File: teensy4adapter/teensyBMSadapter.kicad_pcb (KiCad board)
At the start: 2 copper layers, 23.2 x 37 mm, 11 parts, among them J1 Conn_01x14_Socket, J2 Conn_01x14_Pin, J3 Conn_01x14_Pin, J4 Conn_01x14_Socket

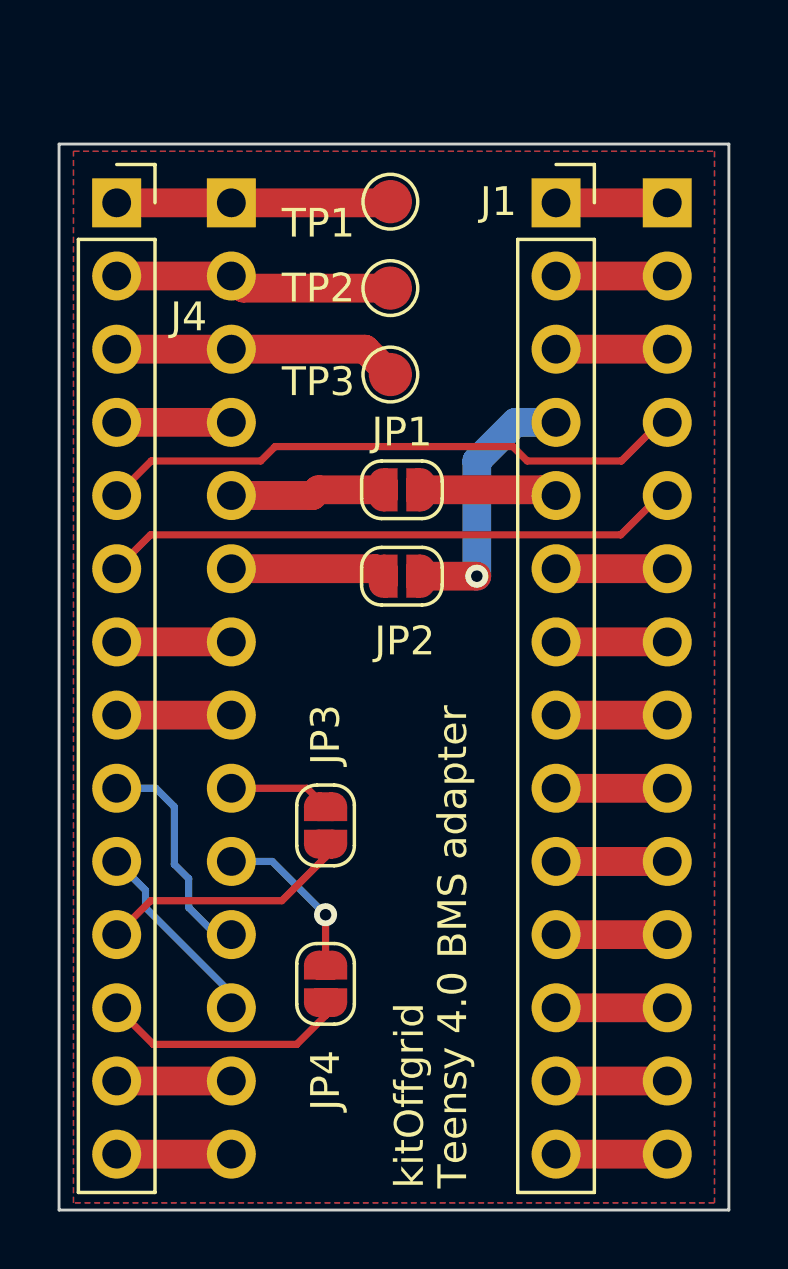
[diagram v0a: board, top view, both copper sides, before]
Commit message: kicad: connected UART3 because of the tesla module.
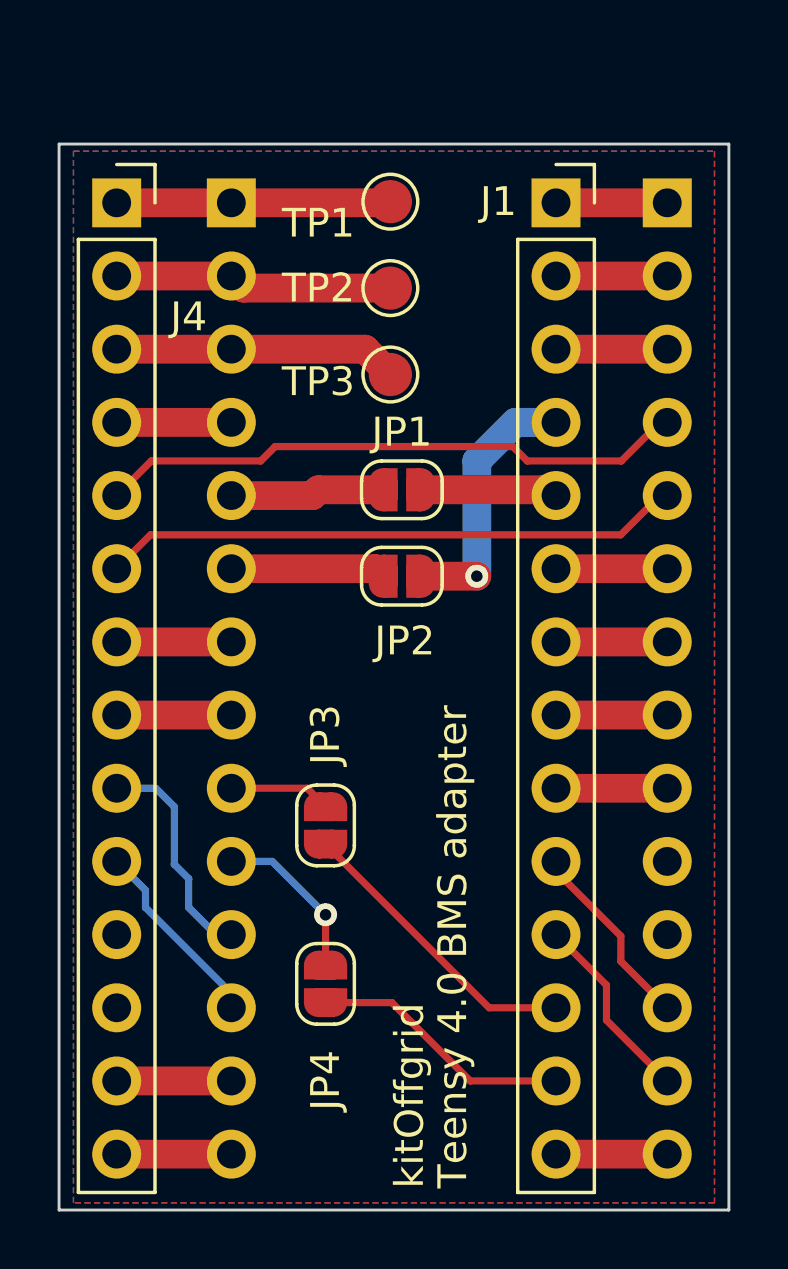
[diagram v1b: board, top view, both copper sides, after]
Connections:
- net Net-(J1-Pin_8) renamed /A5
- net Net-(J1-Pin_9) renamed /A4
- net Net-(J2-Pin_10) renamed /TX3
- net Net-(J2-Pin_9) renamed /RX3
- J1 pad 10: Net-(J1-Pin_10) -> /A3
- J1 pad 11: Net-(J1-Pin_11) -> /A2
- J1 pad 12: /A1 -> /RX3T4
- J1 pad 13: /A0 -> /TX3T4
- J3 pad 10: Net-(J1-Pin_10) -> /P17
- J3 pad 11: Net-(J1-Pin_11) -> /P18
- J3 pad 12: /A1 -> /A3
- J3 pad 13: /A0 -> /A2
- JP3 pad 1: /IO3 -> /RX3T4
- JP4 pad 1: /CS -> /TX3T4
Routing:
- net /RX3T4: track 0.00 -> 10.4 mm
- net /TX3T4: track 0.00 -> 9.13 mm
- net /IO3: track 8.81 -> 0.00 mm
- net /CS: track 8.64 -> 0.00 mm
- net /A3: track 0.00 -> 6.68 mm
- net /A2: track 0.00 -> 6.68 mm
- net Net-(J1-Pin_11): track 3.86 -> 0.00 mm
- net Net-(J1-Pin_10): track 3.86 -> 0.00 mm
- net /A1: track 3.86 -> 0.00 mm
- net /A0: track 3.86 -> 0.00 mm
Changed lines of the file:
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@@
   (net 6 "/A7")
   (net 7 "/A6")
-  (net 8 "Net-(J1-Pin_8)")
-  (net 9 "Net-(J1-Pin_9)")
-  (net 10 "Net-(J1-Pin_10)")
-  (net 11 "Net-(J1-Pin_11)")
-  (net 12 "/A1")
-  (net 13 "/A0")
+  (net 8 "/A5")
+  (net 9 "/A4")
+  (net 10 "/A3")
+  (net 11 "/A2")
+  (net 12 "/RX3T4")
+  (net 13 "/TX3T4")
   (net 14 "/LED{slash}SCK")
   (net 15 "/GND")
@@
   (net 29 "Net-(J2-Pin_5)")
   (net 30 "Net-(J2-Pin_6)")
-  (net 31 "Net-(J2-Pin_9)")
-  (net 32 "Net-(J2-Pin_10)")
+  (net 31 "/RX3")
+  (net 32 "/TX3")
+  (net 33 "/P17")
+  (net 34 "/P18")
   (footprint "Jumper:SolderJumper-2_P1.3mm_Open_RoundedPad1.0x1.5mm" (layer "F.Cu")
     (at 138.75 87.65 90)
@@
       (stroke (width 0.05) (type solid)) (layer "F.CrtYd"))
     (pad "1" smd custom (at -0.65 0 90) (size 1 0.5) (layers "F.Cu" "F.Mask")
-      (net 21 "/IO3") (pinfunction "A") (pintype "passive") (zone_connect 2) (thermal_bridge_angle 45)
+      (net 12 "/RX3T4") (pinfunction "A") (pintype "passive") (zone_connect 2) (thermal_bridge_angle 45)
       (options (clearance outline) (anchor rect))
       (primitives
@@
       ))
     (pad "2" smd custom (at 0.65 0 90) (size 1 0.5) (layers "F.Cu" "F.Mask")
-      (net 31 "Net-(J2-Pin_9)") (pinfunction "B") (pintype "passive") (zone_connect 2) (thermal_bridge_angle 45)
+      (net 31 "/RX3") (pinfunction "B") (pintype "passive") (zone_connect 2) (thermal_bridge_angle 45)
       (options (clearance outline) (anchor rect))
       (primitives
@@
       (stroke (width 0.05) (type solid)) (layer "F.CrtYd"))
     (pad "1" smd custom (at -0.65 0 90) (size 1 0.5) (layers "F.Cu" "F.Mask")
-      (net 22 "/CS") (pinfunction "A") (pintype "passive") (zone_connect 2) (thermal_bridge_angle 45)
+      (net 13 "/TX3T4") (pinfunction "A") (pintype "passive") (zone_connect 2) (thermal_bridge_angle 45)
       (options (clearance outline) (anchor rect))
       (primitives
@@
       ))
     (pad "2" smd custom (at 0.65 0 90) (size 1 0.5) (layers "F.Cu" "F.Mask")
-      (net 32 "Net-(J2-Pin_10)") (pinfunction "B") (pintype "passive") (zone_connect 2) (thermal_bridge_angle 45)
+      (net 32 "/TX3") (pinfunction "B") (pintype "passive") (zone_connect 2) (thermal_bridge_angle 45)
       (options (clearance outline) (anchor rect))
       (primitives
@@
       (net 7 "/A6") (pinfunction "Pin_7") (pintype "passive"))
     (pad "8" thru_hole oval (at 0 17.78) (size 1.7 1.7) (drill 1) (layers "*.Cu" "*.Mask")
-      (net 8 "Net-(J1-Pin_8)") (pinfunction "Pin_8") (pintype "passive"))
+      (net 8 "/A5") (pinfunction "Pin_8") (pintype "passive"))
     (pad "9" thru_hole oval (at 0 20.32) (size 1.7 1.7) (drill 1) (layers "*.Cu" "*.Mask")
-      (net 9 "Net-(J1-Pin_9)") (pinfunction "Pin_9") (pintype "passive"))
+      (net 9 "/A4") (pinfunction "Pin_9") (pintype "passive"))
     (pad "10" thru_hole oval (at 0 22.86) (size 1.7 1.7) (drill 1) (layers "*.Cu" "*.Mask")
-      (net 10 "Net-(J1-Pin_10)") (pinfunction "Pin_10") (pintype "passive"))
+      (net 10 "/A3") (pinfunction "Pin_10") (pintype "passive"))
     (pad "11" thru_hole oval (at 0 25.4) (size 1.7 1.7) (drill 1) (layers "*.Cu" "*.Mask")
-      (net 11 "Net-(J1-Pin_11)") (pinfunction "Pin_11") (pintype "passive"))
+      (net 11 "/A2") (pinfunction "Pin_11") (pintype "passive"))
     (pad "12" thru_hole oval (at 0 27.94) (size 1.7 1.7) (drill 1) (layers "*.Cu" "*.Mask")
-      (net 12 "/A1") (pinfunction "Pin_12") (pintype "passive"))
+      (net 12 "/RX3T4") (pinfunction "Pin_12") (pintype "passive"))
     (pad "13" thru_hole oval (at 0 30.48) (size 1.7 1.7) (drill 1) (layers "*.Cu" "*.Mask")
-      (net 13 "/A0") (pinfunction "Pin_13") (pintype "passive"))
+      (net 13 "/TX3T4") (pinfunction "Pin_13") (pintype "passive"))
     (pad "14" thru_hole oval (at 0 33.02) (size 1.7 1.7) (drill 1) (layers "*.Cu" "*.Mask")
       (net 14 "/LED{slash}SCK") (pinfunction "Pin_14") (pintype "passive"))
@@
       (net 20 "Net-(J2-Pin_8)") (pinfunction "Pin_8") (pintype "passive"))
     (pad "9" thru_hole oval (at 0 -20.32 180) (size 1.7 1.7) (drill 1) (layers "*.Cu" "*.Mask")
-      (net 31 "Net-(J2-Pin_9)") (pinfunction "Pin_9") (pintype "passive"))
+      (net 31 "/RX3") (pinfunction "Pin_9") (pintype "passive"))
     (pad "10" thru_hole oval (at 0 -22.86 180) (size 1.7 1.7) (drill 1) (layers "*.Cu" "*.Mask")
-      (net 32 "Net-(J2-Pin_10)") (pinfunction "Pin_10") (pintype "passive"))
+      (net 32 "/TX3") (pinfunction "Pin_10") (pintype "passive"))
     (pad "11" thru_hole oval (at 0 -25.4 180) (size 1.7 1.7) (drill 1) (layers "*.Cu" "*.Mask")
       (net 23 "Net-(J2-Pin_11)") (pinfunction "Pin_11") (pintype "passive"))
@@
       (net 7 "/A6") (pinfunction "Pin_7") (pintype "passive"))
     (pad "8" thru_hole oval (at 0 -17.78 180) (size 1.7 1.7) (drill 1) (layers "*.Cu" "*.Mask")
-      (net 8 "Net-(J1-Pin_8)") (pinfunction "Pin_8") (pintype "passive"))
+      (net 8 "/A5") (pinfunction "Pin_8") (pintype "passive"))
     (pad "9" thru_hole oval (at 0 -20.32 180) (size 1.7 1.7) (drill 1) (layers "*.Cu" "*.Mask")
-      (net 9 "Net-(J1-Pin_9)") (pinfunction "Pin_9") (pintype "passive"))
+      (net 9 "/A4") (pinfunction "Pin_9") (pintype "passive"))
     (pad "10" thru_hole oval (at 0 -22.86 180) (size 1.7 1.7) (drill 1) (layers "*.Cu" "*.Mask")
-      (net 10 "Net-(J1-Pin_10)") (pinfunction "Pin_10") (pintype "passive"))
+      (net 33 "/P17") (pinfunction "Pin_10") (pintype "passive"))
     (pad "11" thru_hole oval (at 0 -25.4 180) (size 1.7 1.7) (drill 1) (layers "*.Cu" "*.Mask")
-      (net 11 "Net-(J1-Pin_11)") (pinfunction "Pin_11") (pintype "passive"))
+      (net 34 "/P18") (pinfunction "Pin_11") (pintype "passive"))
     (pad "12" thru_hole oval (at 0 -27.94 180) (size 1.7 1.7) (drill 1) (layers "*.Cu" "*.Mask")
-      (net 12 "/A1") (pinfunction "Pin_12") (pintype "passive"))
+      (net 10 "/A3") (pinfunction "Pin_12") (pintype "passive"))
     (pad "13" thru_hole oval (at 0 -30.48 180) (size 1.7 1.7) (drill 1) (layers "*.Cu" "*.Mask")
-      (net 13 "/A0") (pinfunction "Pin_13") (pintype "passive"))
+      (net 11 "/A2") (pinfunction "Pin_13") (pintype "passive"))
     (pad "14" thru_hole oval (at 0 -33.02 180) (size 1.7 1.7) (drill 1) (layers "*.Cu" "*.Mask")
       (net 14 "/LED{slash}SCK") (pinfunction "Pin_14") (pintype "passive"))
@@
   (segment (start 146.5 83.82) (end 150.36 83.82) (width 1) (layer "F.Cu") (net 8))
   (segment (start 150.36 86.36) (end 146.5 86.36) (width 1) (layer "F.Cu") (net 9))
-  (segment (start 146.5 88.9) (end 150.36 88.9) (width 1) (layer "F.Cu") (net 10))
-  (segment (start 150.36 91.44) (end 146.5 91.44) (width 1) (layer "F.Cu") (net 11))
-  (segment (start 146.5 93.98) (end 150.36 93.98) (width 1) (layer "F.Cu") (net 12))
-  (segment (start 150.36 96.52) (end 146.5 96.52) (width 1) (layer "F.Cu") (net 13))
+  (segment (start 149 91.491701) (end 149 92.37) (width 0.25) (layer "F.Cu") (net 10))
+  (segment (start 146.75 88.9) (end 146.75 89.241701) (width 0.25) (layer "F.Cu") (net 10))
+  (segment (start 146.75 89.241701) (end 149 91.491701) (width 0.25) (layer "F.Cu") (net 10))
+  (segment (start 149 92.37) (end 150.61 93.98) (width 0.25) (layer "F.Cu") (net 10))
+  (segment (start 148.5 93.19) (end 146.75 91.44) (width 0.25) (layer "F.Cu") (net 11))
+  (segment (start 150.61 96.52) (end 148.5 94.41) (width 0.25) (layer "F.Cu") (net 11))
+  (segment (start 148.5 94.41) (end 148.5 93.19) (width 0.25) (layer "F.Cu") (net 11))
+  (segment (start 138.75 88.3) (end 144.43 93.98) (width 0.25) (layer "F.Cu") (net 12))
+  (segment (start 144.43 93.98) (end 146.75 93.98) (width 0.25) (layer "F.Cu") (net 12))
+  (segment (start 138.75 93.8) (end 141.05 93.8) (width 0.25) (layer "F.Cu") (net 13))
+  (segment (start 141.05 93.8) (end 143.77 96.52) (width 0.25) (layer "F.Cu") (net 13))
+  (segment (start 143.77 96.52) (end 146.75 96.52) (width 0.25) (layer "F.Cu") (net 13))
   (segment (start 146.5 99.06) (end 150.36 99.06) (width 1) (layer "F.Cu") (net 14))
   (segment (start 131.5 66.04) (end 135.48 66.04) (width 1) (layer "F.Cu") (net 15))
@@
   (segment (start 131.5 81.28) (end 135.48 81.28) (width 1) (layer "F.Cu") (net 19))
   (segment (start 135.48 83.82) (end 131.5 83.82) (width 1) (layer "F.Cu") (net 20))
-  (segment (start 138.75 88.3) (end 138.75 88.75) (width 0.25) (layer "F.Cu") (net 21))
-  (segment (start 137.235 90.265) (end 132.675 90.265) (width 0.25) (layer "F.Cu") (net 21))
-  (segment (start 138.75 88.75) (end 137.235 90.265) (width 0.25) (layer "F.Cu") (net 21))
-  (segment (start 132.675 90.265) (end 131.5 91.44) (width 0.25) (layer "F.Cu") (net 21))
-  (segment (start 137.75 95.25) (end 132.77 95.25) (width 0.25) (layer "F.Cu") (net 22))
-  (segment (start 138.75 94.25) (end 137.75 95.25) (width 0.25) (layer "F.Cu") (net 22))
-  (segment (start 138.75 93.8) (end 138.75 94.25) (width 0.25) (layer "F.Cu") (net 22))
-  (segment (start 132.77 95.25) (end 131.5 93.98) (width 0.25) (layer "F.Cu") (net 22))
   (segment (start 134 89.5) (end 134 90.5) (width 0.25) (layer "B.Cu") (net 23))
   (segment (start 133.5 89) (end 134 89.5) (width 0.25) (layer "B.Cu") (net 23))

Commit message: Adding closed solder jumpers to the CAN bus pins
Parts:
- removed JP2: SolderJumper_2_Open, Jumper:SolderJumper-2_P1.3mm_Open_RoundedPad1.0x1.5mm
- added JP5: SolderJumper_2_Open, Jumper:SolderJumper-2_P1.3mm_Open_RoundedPad1.0x1.5mm, F.Cu at (141.5, 84.1)
- added JP6: SolderJumper_2_Open, Jumper:SolderJumper-2_P1.3mm_Open_RoundedPad1.0x1.5mm, F.Cu at (142.1, 88.2)
- added JP7: SolderJumper_2_Bridged, Jumper:SolderJumper-2_P1.3mm_Bridged_RoundedPad1.0x1.5mm, F.Cu at (141.3, 76.0)
- JP1: value SolderJumper_2_Open -> SolderJumper_2_Bridged; footprint Jumper:SolderJumper-2_P1.3mm_Open_RoundedPad1.0x1.5mm -> Jumper:SolderJumper-2_P1.3mm_Bridged_RoundedPad1.0x1.5mm
- moved JP1 3.00 mm to (141.3, 79.0)
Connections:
- JP1 pad 1: /CANTX1 -> /CANRX1
- JP1 pad 2: Net-(J2-Pin_5) -> Net-(J2-Pin_6)
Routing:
- net /CS: track 0.00 -> 15.1 mm, vias 0 -> 1
- net /IO3: track 0.00 -> 14.4 mm
- net /P17: track 0.00 -> 11.8 mm, vias 0 -> 1
- net /P18: track 0.00 -> 9.52 mm, vias 0 -> 1
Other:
- board text added: "Teensy 4.0 SIMPBMS adapter"
- board text removed: "Teensy 4.0 BMS adapter"
